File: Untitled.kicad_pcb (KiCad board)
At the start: 2 copper layers, 37 x 37 mm, 22 parts, among them J1 Battery Connector, J2 Top Screw Terminal, J3 Bottom Screw Terminal, Q1 Q_NMOS_DGS, Q2 Q_NMOS_DGS, Q3 Q_NMOS_DGS, U1 XIAO-ESP32-S3-SMD, U3 LSM6DSO32, U4 MS5611-01BA

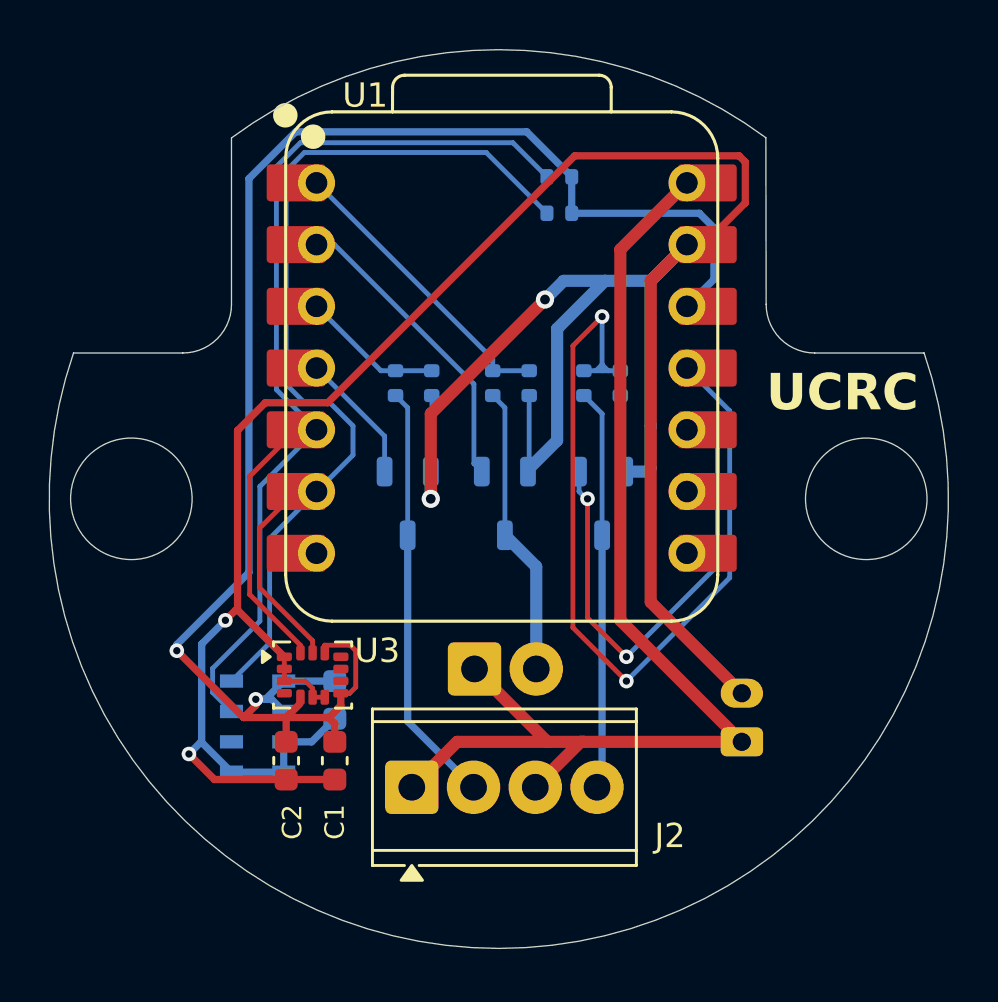
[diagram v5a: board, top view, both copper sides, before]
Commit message: Silkscreen and Cleanup
Added needed silkscreen elements like screw terminal labels and IMU axis indicator. Also added some UCRC related text and added (placeholder for now) avionics team member names below ESP32 cutout.
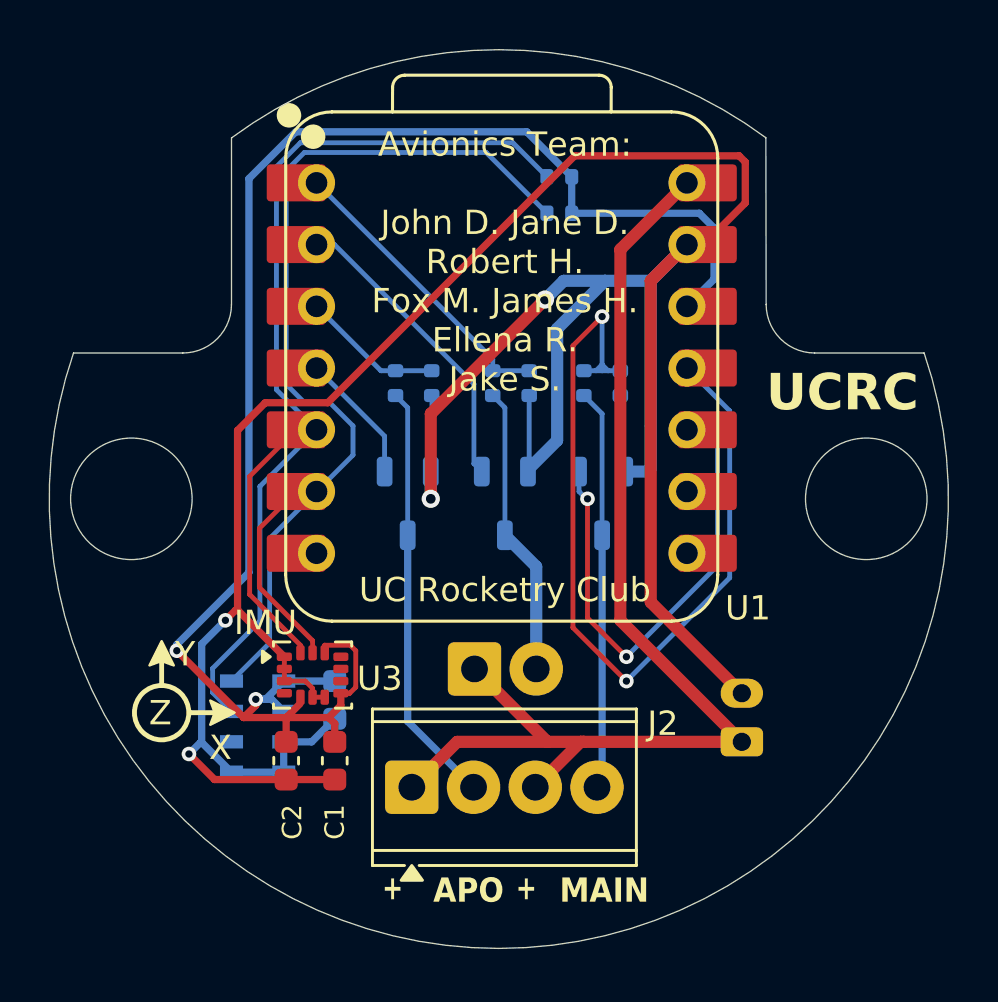
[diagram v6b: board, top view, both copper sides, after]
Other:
- board text added: "+"
- board text added: "-"
- board text added: "5V Max"
- board text added: "APO"
- board text added: "Avionics Team: John D. Jane D. Robert H. Fox M. James H. Ellena R. Jake S."
- board text added: "Baro"
- board text added: "Batt. In"
- board text added: "Double or Nothing!"
- board text added: "IMU"
- board text added: "MAIN"
- board text added: "MOTOR"
- board text added: "UC Rocketry Club"
- board text added: "X"
- board text added: "Y"
- board text added: "Z"

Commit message: Small Silkscreen Changes
Added indicator for intended direction and made part label formatting consistent. Also added Jebediah Kerman to the list of fake names
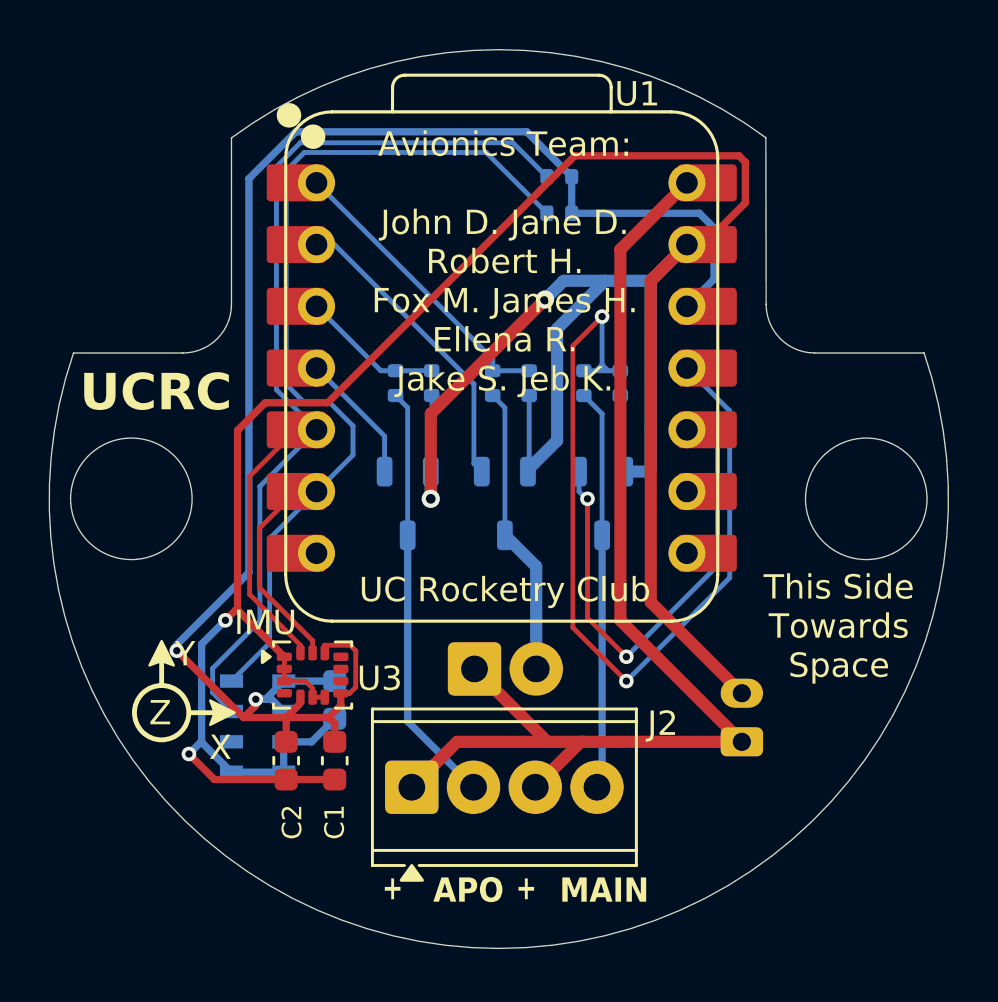
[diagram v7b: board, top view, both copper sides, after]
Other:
- board text added: "Avionics Team: John D. Jane D. Robert H. Fox M. James H. Ellena R. Jake S. Jeb K."
- board text added: "This Side Towards Space"
- board text removed: "Avionics Team: John D. Jane D. Robert H. Fox M. James H. Ellena R. Jake S."
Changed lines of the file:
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@@
 		(at 206.12 62.12)
 		(property "Reference" "U1"
-			(at 10.13 9.88 0)
+			(at 5.58 -11.27 0)
 			(unlocked yes)
 			(layer "F.SilkS")
@@
 			(effects
 				(font
-					(size 1 1)
+					(size 0.8 0.8)
 					(thickness 0.15)
 				)
@@
 			(effects
 				(font
-					(size 1 1)
+					(size 0.8 0.8)
 					(thickness 0.15)
 				)
@@
 			(effects
 				(font
-					(size 1 1)
+					(size 0.8 0.8)
 					(thickness 0.15)
 				)
@@
 	)
 	(gr_text "UCRC"
-		(at 217 64 0)
+		(at 188.75 64 0)
 		(layer "F.SilkS")
 		(effects
@@
 		)
 	)
-	(gr_text "Avionics Team:\n\nJohn D. Jane D.\nRobert H.\nFox M. James H.\nEllena R.\nJake S. "
+	(gr_text "This Side\nTowards\nSpace"
+		(at 220 72.75 0)
+		(layer "F.SilkS")
+		(effects
+			(font
+				(size 1 1)
+				(thickness 0.15)
+			)
+		)
+	)
+	(gr_text "Avionics Team:\n\nJohn D. Jane D.\nRobert H.\nFox M. James H.\nEllena R.\nJake S. Jeb K."
 		(at 206.25 57.75 0)
 		(layer "F.SilkS")
